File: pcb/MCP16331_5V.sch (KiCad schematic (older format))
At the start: 12 parts, among them U8 MCP16331T

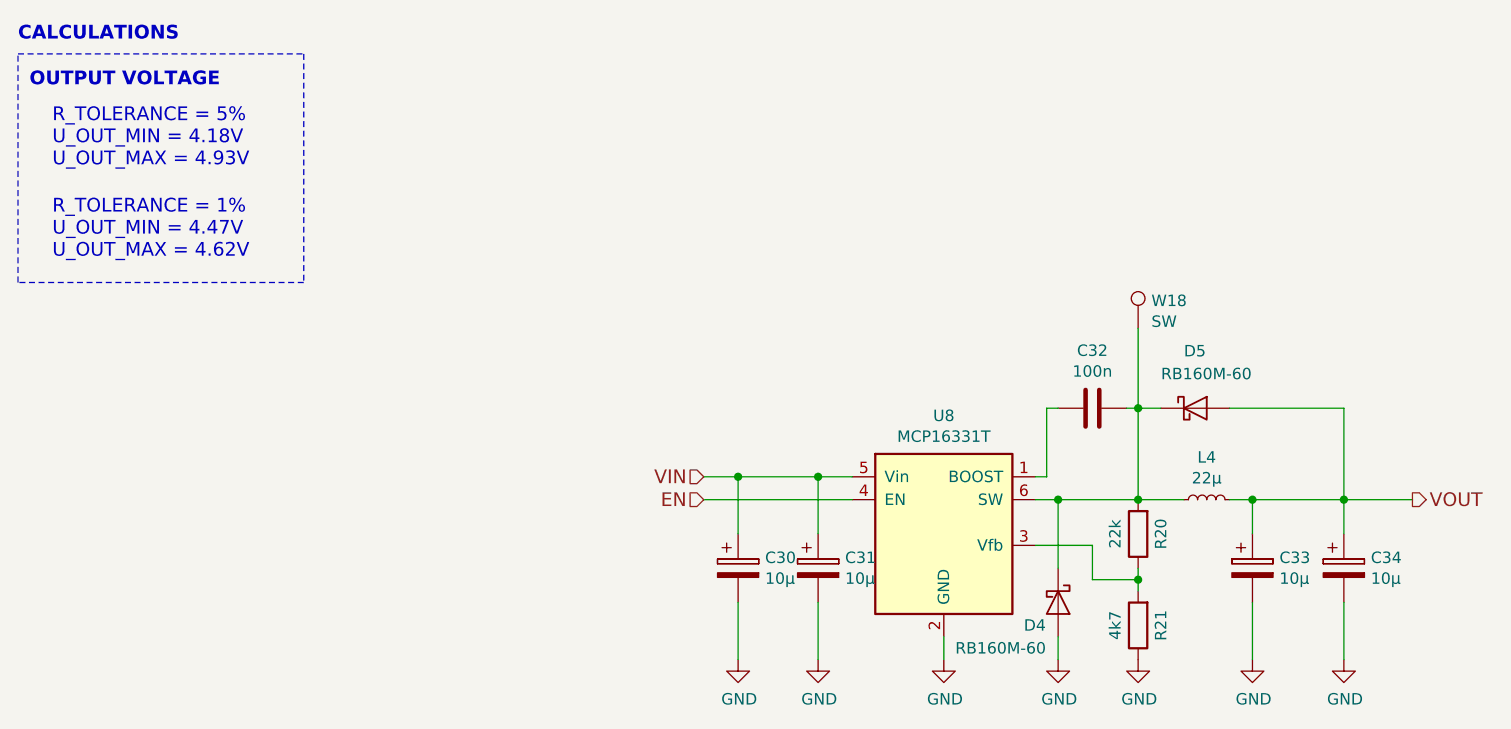
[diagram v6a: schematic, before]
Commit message: Use new library symbols
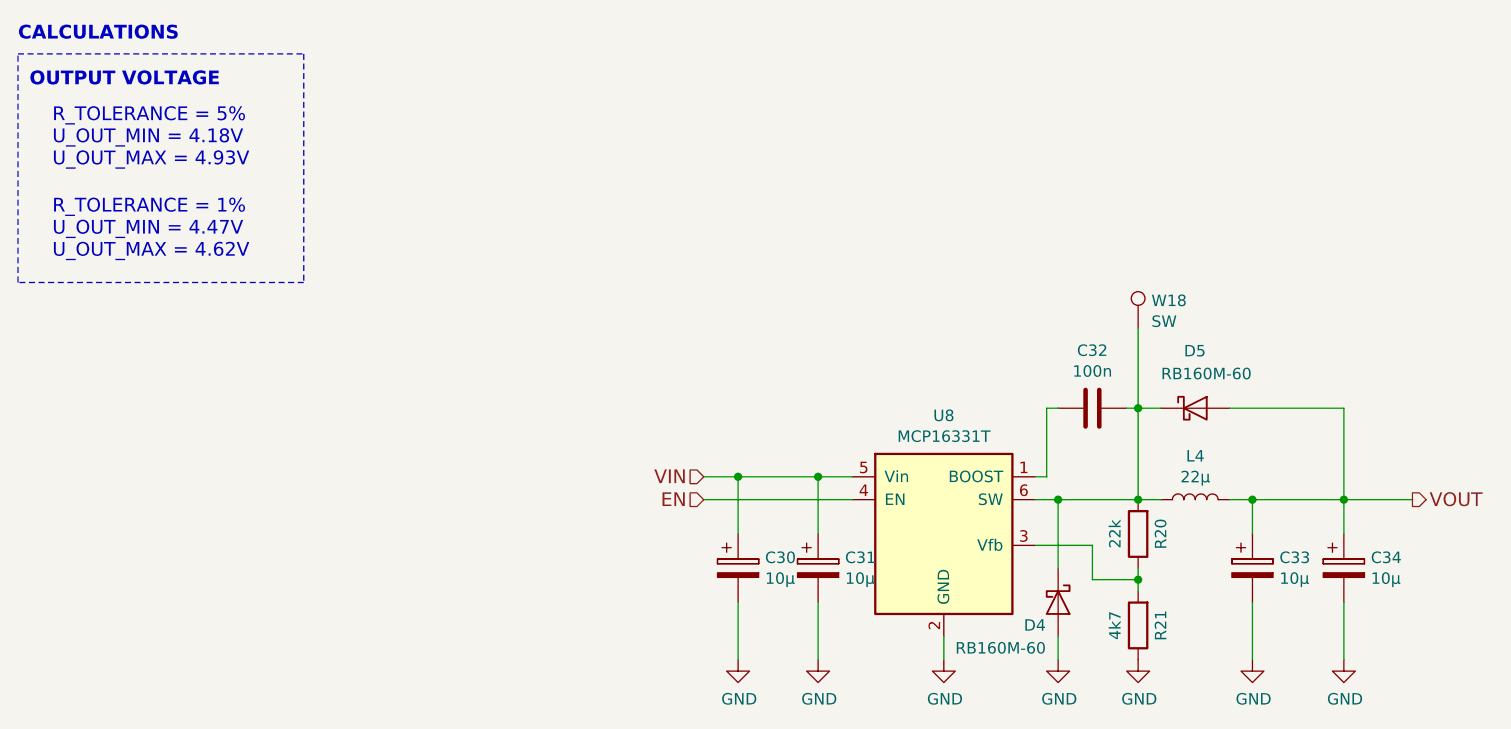
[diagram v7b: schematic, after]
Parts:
- removed L4: 22µ, Inductors_local:Inductor_Würth_SPC_4818, symbol INDUCTOR_Small
- added L4: 22µ, Inductors_local:Inductor_Würth_SPC_4818, symbol L
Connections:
- net VOUT: now also L4.2
- net at C32.2, D4.1 (K), D5.1 (K)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: now also L4.1
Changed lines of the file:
@@
 	5300 4050 5300 4150
-$Comp
-L INDUCTOR_Small L4
-U 1 1 580BA381
-P 6450 3450
-F 0 "L4" V 6635 3450 50  0000 C CNN
-F 1 "22µ" V 6544 3450 50  0000 C CNN
-F 2 "Inductors_local:Inductor_Würth_SPC_4818" H 6450 3450 50  0001 C CNN
-F 3 "http://katalog.we-online.de/pbs/datasheet/744773122.pdf" H 6450 3450 50  0001 C CNN
-F 4 "732-1258-1-ND" V 6450 3450 60  0001 C CNN "Digi-Key Part Number"
-F 5 "1" V 6450 3450 60  0001 C CNN "Digi-Key Minimum Quantity"
-	1    6450 3450
-	0    -1   -1   0
-$EndComp
 $Comp
 L CP C31
@@
 $EndComp
 Wire Wire Line
-	5700 3450 6350 3450
-Wire Wire Line
-	6100 3050 6250 3050
-Wire Wire Line
-	6150 2700 6150 3450
+	5700 3450 5800 3450
+Wire Wire Line
+	5800 3450 6150 3450
+Wire Wire Line
+	6150 3450 6250 3450
+Wire Wire Line
+	6100 3050 6150 3050
+Wire Wire Line
+	6150 3050 6250 3050
+Wire Wire Line
+	6150 2700 6150 3050
+Wire Wire Line
+	6150 3050 6150 3450
 Connection ~ 6150 3450
 Wire Wire Line
@@
 $EndComp
 Wire Wire Line
-	6150 3750 6150 3850
+	6150 3750 6150 3800
+Wire Wire Line
+	6150 3800 6150 3850
 Wire Wire Line
 	5700 3650 5950 3650
@@
 	6550 3050 7050 3050
 Wire Wire Line
-	7050 3050 7050 3600
-Wire Wire Line
-	6550 3450 7350 3450
+	7050 3050 7050 3450
+Wire Wire Line
+	7050 3450 7050 3600
+Wire Wire Line
+	6550 3450 6650 3450
+Wire Wire Line
+	6650 3450 7050 3450
+Wire Wire Line
+	7050 3450 7350 3450
 Wire Wire Line
 	6650 3450 6650 3600
@@
 VOUT
 Wire Wire Line
-	4250 3350 4900 3350
+	4250 3350 4400 3350
+Wire Wire Line
+	4400 3350 4750 3350
+Wire Wire Line
+	4750 3350 4900 3350
 Wire Wire Line
 	4400 3350 4400 3600
@@
 Wire Notes Line
 	1250 2500 1250 1500
+$Comp
+L L L4
+U 1 1 582ECCE6
+P 6400 3450
+F 0 "L4" V 6590 3450 50  0000 C CNN
+F 1 "22µ" V 6499 3450 50  0000 C CNN
+F 2 "Inductors_local:Inductor_Würth_SPC_4818" V 6498 3450 50  0001 C CNN
+F 3 "http://katalog.we-online.de/pbs/datasheet/744773122.pdf" V 6498 3450 50  0001 C CNN
+F 4 "732-1258-1-ND" H 6400 3450 60  0001 C CNN "Digi-Key Part Number"
+F 5 "1" H 6400 3450 60  0001 C CNN "Digi-Key Minimum Quantity"
+	1    6400 3450
+	0    -1   -1   0
+$EndComp
 $EndSCHEMATC

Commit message: Improve pcb routing
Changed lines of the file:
@@
 $EndComp
 Wire Wire Line
-	5700 3450 5800 3450
+	5700 3450 6250 3450
 Wire Wire Line
-	5800 3450 6150 3450
+	6100 3050 6250 3050
 Wire Wire Line
-	6150 3450 6250 3450
-Wire Wire Line
-	6100 3050 6150 3050
-Wire Wire Line
-	6150 3050 6250 3050
-Wire Wire Line
-	6150 2700 6150 3050
-Wire Wire Line
-	6150 3050 6150 3450
+	6150 2700 6150 3450
 Connection ~ 6150 3450
 Wire Wire Line
@@
 $EndComp
 Wire Wire Line
-	6150 3750 6150 3800
-Wire Wire Line
-	6150 3800 6150 3850
+	6150 3750 6150 3850
 Wire Wire Line
 	5700 3650 5950 3650
@@
 	6550 3050 7050 3050
 Wire Wire Line
-	7050 3050 7050 3450
+	7050 3050 7050 3600
 Wire Wire Line
-	7050 3450 7050 3600
-Wire Wire Line
-	6550 3450 6650 3450
-Wire Wire Line
-	6650 3450 7050 3450
-Wire Wire Line
-	7050 3450 7350 3450
+	6550 3450 7350 3450
 Wire Wire Line
 	6650 3450 6650 3600
@@
 VOUT
 Wire Wire Line
-	4250 3350 4400 3350
-Wire Wire Line
-	4400 3350 4750 3350
-Wire Wire Line
-	4750 3350 4900 3350
+	4250 3350 4900 3350
 Wire Wire Line
 	4400 3350 4400 3600
